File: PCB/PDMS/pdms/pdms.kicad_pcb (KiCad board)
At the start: 2 copper layers, 31 parts, among them IC1 BTS500101TAEATMA1, IC2 BTS500101TAEATMA1, IC3 BTS500101TAEATMA1, IC4 BTS500101TAEATMA1, IC5 BTS500101TAEATMA1, IC6 BTS500101TAEATMA1, IC7 BTS722204ESAXUMA1, IC8 BTS500101TAEATMA1, IC9 BTS500101TAEATMA1

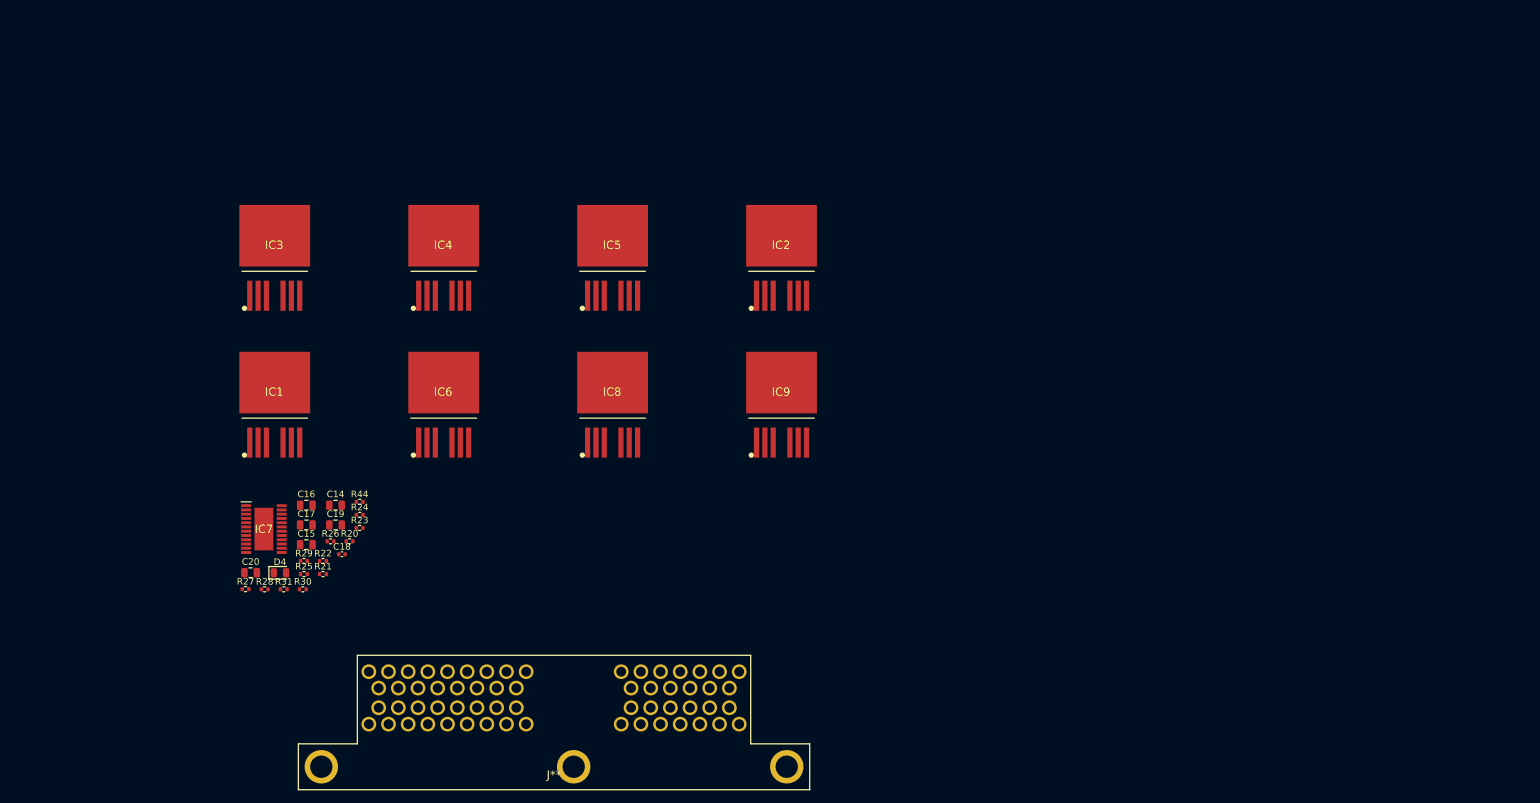
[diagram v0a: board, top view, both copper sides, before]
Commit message: Added MCU section
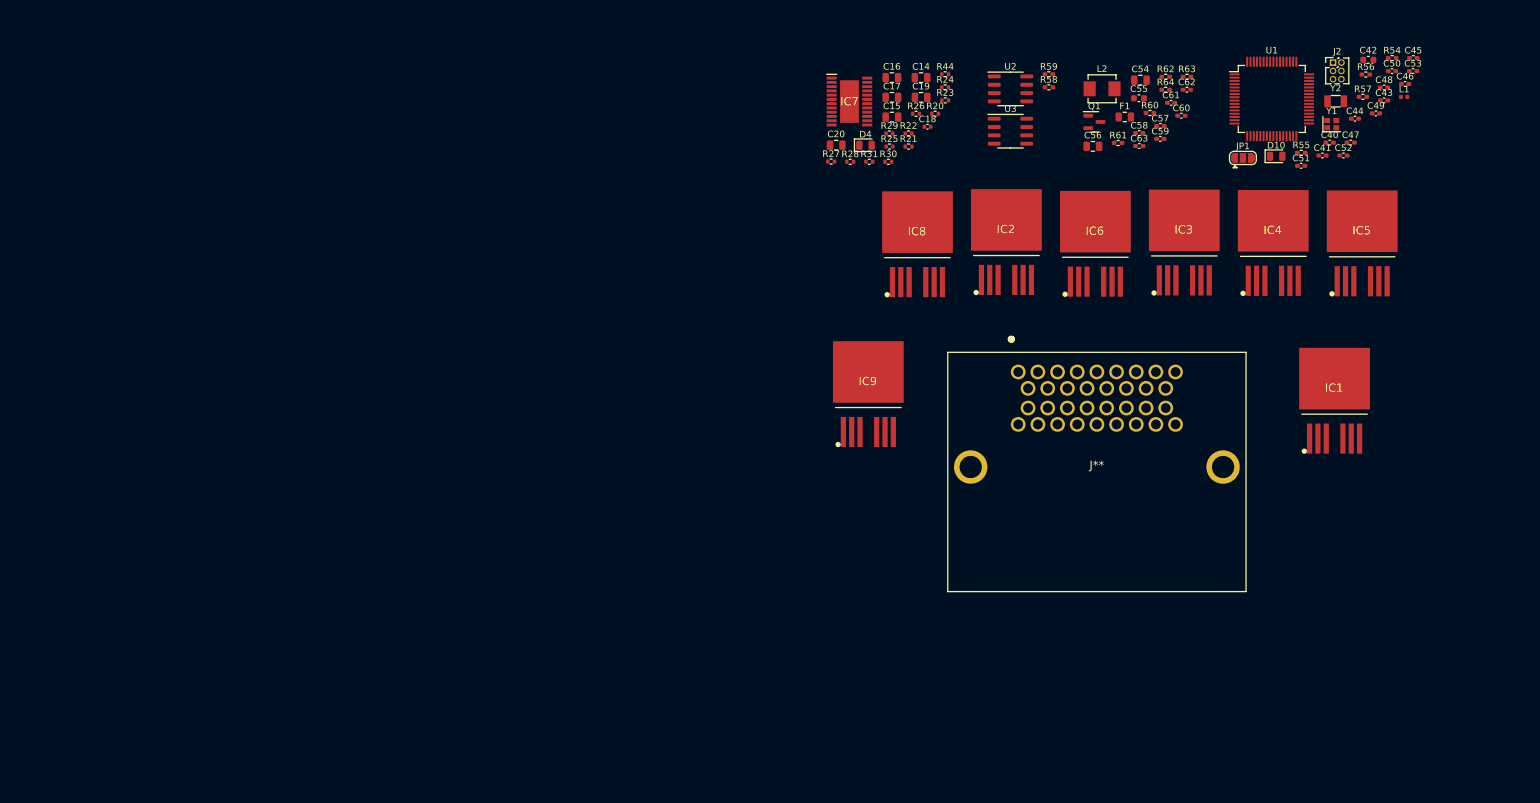
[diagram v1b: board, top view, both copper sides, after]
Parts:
- removed the J** at (76.2, 114.3)
- added C40: 2u2, Capacitor_SMD:C_0402_1005Metric_Pad0.74x0.62mm_HandSolder, F.Cu at (222.8, 33.6)
- added C41: 2u2, Capacitor_SMD:C_0402_1005Metric_Pad0.74x0.62mm_HandSolder, F.Cu at (221.7, 35.6)
- added C42: 4,7uF, Capacitor_SMD:C_0603_1608Metric, F.Cu at (228.7, 21.0)
- added C43: 100nF, Capacitor_SMD:C_0402_1005Metric_Pad0.74x0.62mm_HandSolder, F.Cu at (231.1, 27.2)
- added C44: 100nF, Capacitor_SMD:C_0402_1005Metric_Pad0.74x0.62mm_HandSolder, F.Cu at (226.6, 29.9)
- added C45: 100nF, Capacitor_SMD:C_0402_1005Metric_Pad0.74x0.62mm_HandSolder, F.Cu at (235.5, 20.7)
- added C46: 100nF, Capacitor_SMD:C_0402_1005Metric_Pad0.74x0.62mm_HandSolder, F.Cu at (234.3, 24.6)
- added C47: 100n, Capacitor_SMD:C_0402_1005Metric_Pad0.74x0.62mm_HandSolder, F.Cu at (226.0, 33.6)
- added C48: 10pF, Capacitor_SMD:C_0402_1005Metric_Pad0.74x0.62mm_HandSolder, F.Cu at (231.1, 25.2)
- added C49: 100n, Capacitor_SMD:C_0402_1005Metric_Pad0.74x0.62mm_HandSolder, F.Cu at (229.8, 29.1)
- added C50: 10pF, Capacitor_SMD:C_0402_1005Metric_Pad0.74x0.62mm_HandSolder, F.Cu at (232.3, 22.7)
- added C51: 1u, Capacitor_SMD:C_0402_1005Metric_Pad0.74x0.62mm_HandSolder, F.Cu at (218.4, 37.1)
- added C52: 10pF, Capacitor_SMD:C_0402_1005Metric_Pad0.74x0.62mm_HandSolder, F.Cu at (224.9, 35.6)
- added C53: 10pF, Capacitor_SMD:C_0402_1005Metric_Pad0.74x0.62mm_HandSolder, F.Cu at (235.5, 22.7)
- added C54: 1uF, Capacitor_SMD:C_0805_2012Metric, F.Cu at (193.9, 24.1)
- added C55: 4.7uF, Capacitor_SMD:C_0603_1608Metric, F.Cu at (193.7, 26.8)
- added C56: 22uF, Capacitor_SMD:C_0805_2012Metric, F.Cu at (186.7, 34.2)
- added C57: 1nF, Capacitor_SMD:C_0402_1005Metric_Pad0.74x0.62mm_HandSolder, F.Cu at (196.9, 31.1)
- added C58: 0.1uF, Capacitor_SMD:C_0402_1005Metric_Pad0.74x0.62mm_HandSolder, F.Cu at (193.7, 32.1)
- added C59: 6.8nF, Capacitor_SMD:C_0402_1005Metric_Pad0.74x0.62mm_HandSolder, F.Cu at (196.9, 33.0)
- added C60: 1uF, Capacitor_SMD:C_0402_1005Metric_Pad0.74x0.62mm_HandSolder, F.Cu at (200.2, 29.5)
- added C61: 10pF, Capacitor_SMD:C_0402_1005Metric_Pad0.74x0.62mm_HandSolder, F.Cu at (198.6, 27.5)
- added C62: 22uF, Capacitor_SMD:C_0402_1005Metric_Pad0.74x0.62mm_HandSolder, F.Cu at (201.0, 25.5)
- added C63: 22uF, Capacitor_SMD:C_0402_1005Metric_Pad0.74x0.62mm_HandSolder, F.Cu at (193.7, 34.1)
- added D10: LED_Small, LED_SMD:LED_0805_2012Metric, F.Cu at (214.6, 35.7)
- added F1: Fuse, Fuse:Fuse_0805_2012Metric, F.Cu at (191.5, 29.7)
- added J**: 64372882, PDMS_Additional:64372882, F.Cu at (175.3, 68.6)
- added J2: DBG, Connector_PinHeader_1.27mm:PinHeader_2x03_P1.27mm_Vertical, F.Cu at (223.3, 21.4)
- added JP1: SolderJumper_3_Open, Jumper:SolderJumper-3_P1.3mm_Open_RoundedPad1.0x1.5mm, F.Cu at (209.5, 35.9)
- added L1: 2u7 120m, Inductor_SMD:L_0402_1005Metric, F.Cu at (234.1, 26.6)
- added L2: 2.2uH, Inductor_SMD:L_Vishay_IHLP-1616, F.Cu at (188.1, 25.4)
- added Q1: AO3401A, Package_TO_SOT_SMD:SOT-23, F.Cu at (186.9, 30.4)
- added R54: 2k2, Resistor_SMD:R_0402_1005Metric_Pad0.72x0.64mm_HandSolder, F.Cu at (232.3, 20.7)
- added R55: 2k2, Resistor_SMD:R_0402_1005Metric_Pad0.72x0.64mm_HandSolder, F.Cu at (218.4, 35.1)
- added R56: 1k5, Resistor_SMD:R_0402_1005Metric_Pad0.72x0.64mm_HandSolder, F.Cu at (228.3, 23.2)
- added R57: 1k, Resistor_SMD:R_0402_1005Metric_Pad0.72x0.64mm_HandSolder, F.Cu at (227.8, 26.6)
- added R58: 120, Resistor_SMD:R_0402_1005Metric_Pad0.72x0.64mm_HandSolder, F.Cu at (179.9, 25.2)
- added R59: 120, Resistor_SMD:R_0402_1005Metric_Pad0.72x0.64mm_HandSolder, F.Cu at (179.9, 23.2)
- added R60: 200k, Resistor_SMD:R_0402_1005Metric_Pad0.72x0.64mm_HandSolder, F.Cu at (195.3, 29.1)
- added R61: 20, Resistor_SMD:R_0402_1005Metric_Pad0.72x0.64mm_HandSolder, F.Cu at (190.5, 33.6)
- added R62: 20k, Resistor_SMD:R_0402_1005Metric_Pad0.72x0.64mm_HandSolder, F.Cu at (197.8, 23.6)
- added R63: 13k, Resistor_SMD:R_0402_1005Metric_Pad0.72x0.64mm_HandSolder, F.Cu at (201.0, 23.6)
- added R64: 40.2k, Resistor_SMD:R_0402_1005Metric_Pad0.72x0.64mm_HandSolder, F.Cu at (197.8, 25.5)
- added U1: STM32F405RGTx, Package_QFP:LQFP-64_10x10mm_P0.5mm, F.Cu at (213.9, 26.9)
- added U2: MCP2561-E-SN, Package_SO:SOIC-8_3.9x4.9mm_P1.27mm, F.Cu at (174.1, 25.4)
- added U3: MCP2561-E-SN, Package_SO:SOIC-8_3.9x4.9mm_P1.27mm, F.Cu at (174.1, 31.9)
- added Y1: 16Mhz, Crystal:Crystal_SMD_2016-4Pin_2.0x1.6mm, F.Cu at (223.1, 30.8)
- added Y2: 32KHz, Crystal:Crystal_SMD_3215-2Pin_3.2x1.5mm, F.Cu at (223.7, 27.3)
- IC1, IC2, IC3, IC4, IC5, IC6, IC8, IC9: footprint PDM_Additional:PG-TO263-7-3_3 -> PDMS_Additional:PG-TO263-7-3_3
- moved IC1 161.7 mm to (223.5, 69.6)
- moved IC3 138.8 mm to (200.6, 45.5)
- moved IC4 126.6 mm to (214.2, 45.5)
- moved IC5 114.4 mm to (227.7, 45.6)
- moved C15 110.6 mm to (156.0, 29.7)
- moved C16 110.6 mm to (156.0, 23.7)
- moved C17 110.6 mm to (156.0, 26.7)
- moved C20 110.6 mm to (147.5, 34.0)
- moved D4 110.6 mm to (152.0, 34.0)
- moved R20 110.6 mm to (162.6, 29.2)
- moved R21 110.6 mm to (158.5, 34.2)
- moved R22 110.6 mm to (158.5, 32.2)
- moved R23 110.6 mm to (164.1, 27.1)
- moved R24 110.6 mm to (164.1, 25.2)
- moved R25 110.6 mm to (155.6, 34.2)
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
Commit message: PDMS schematic update
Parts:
- added BZ1: Buzzer, Buzzer_Beeper:Buzzer_Murata_PKLCS1212E, F.Cu at (245.1, 30.5)
- added D11: WS2812B, LED_SMD:LED_WS2812B-2020_PLCC4_2.0x2.0mm, F.Cu at (183.5, 16.9)
- added D12: WS2812B, LED_SMD:LED_WS2812B-2020_PLCC4_2.0x2.0mm, F.Cu at (194.6, 16.9)
- added D13: WS2812B, LED_SMD:LED_WS2812B-2020_PLCC4_2.0x2.0mm, F.Cu at (189.1, 16.9)
- added D14: WS2812B, LED_SMD:LED_WS2812B-2020_PLCC4_2.0x2.0mm, F.Cu at (178.0, 16.9)
- added D15: WS2812B, LED_SMD:LED_WS2812B-2020_PLCC4_2.0x2.0mm, F.Cu at (200.2, 16.9)
- added D16: WS2812B, LED_SMD:LED_WS2812B-2020_PLCC4_2.0x2.0mm, F.Cu at (172.4, 16.9)
- added D17: WS2812B, LED_SMD:LED_WS2812B-2020_PLCC4_2.0x2.0mm, F.Cu at (205.7, 16.9)
- added D18: WS2812B, LED_SMD:LED_WS2812B-2020_PLCC4_2.0x2.0mm, F.Cu at (166.8, 16.9)
- added D19: WS2812B, LED_SMD:LED_WS2812B-2020_PLCC4_2.0x2.0mm, F.Cu at (161.3, 16.9)
- added IC12: TMP126NDCKR, PDM_Additional:SOT65P210X110-6N, F.Cu at (167.6, 38.1)
- added IC13: TMP126NDCKR, PDM_Additional:SOT65P210X110-6N, F.Cu at (162.6, 38.1)
- added IC14: TMP126NDCKR, PDM_Additional:SOT65P210X110-6N, F.Cu at (162.4, 33.9)
- added Q2: MMBT3904, Package_TO_SOT_SMD:SOT-23, F.Cu at (149.9, 19.1)
- added R65: 10k, Resistor_SMD:R_0402_1005Metric, F.Cu at (161.3, 40.9)
- added R66: 10k, Resistor_SMD:R_0402_1005Metric, F.Cu at (164.2, 40.9)
- added R67: 10k, Resistor_SMD:R_0402_1005Metric, F.Cu at (166.1, 33.0)
- added R72: 1k, Resistor_SMD:R_0402_1005Metric, F.Cu at (156.6, 20.0)
- moved IC2 6.49 mm to (167.6, 48.1)
- moved IC3 6.49 mm to (194.7, 48.2)
- moved IC5 6.49 mm to (221.8, 48.3)
- moved IC6 6.49 mm to (181.1, 48.4)
- moved IC4 6.49 mm to (208.3, 48.3)
- moved IC8 6.49 mm to (154.0, 48.5)
- moved C51 6.49 mm to (212.5, 39.9)
- moved R27 3.27 mm to (144.9, 39.2)
- moved R28 3.27 mm to (147.8, 39.2)
- moved R30 3.27 mm to (153.7, 39.2)
- moved R31 3.27 mm to (150.8, 39.2)
- moved IC1 2.54 mm to (221.0, 69.6)
- moved IC9 1.27 mm to (153.7, 68.6)
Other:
- board outline added: 91.4 x 66 mm

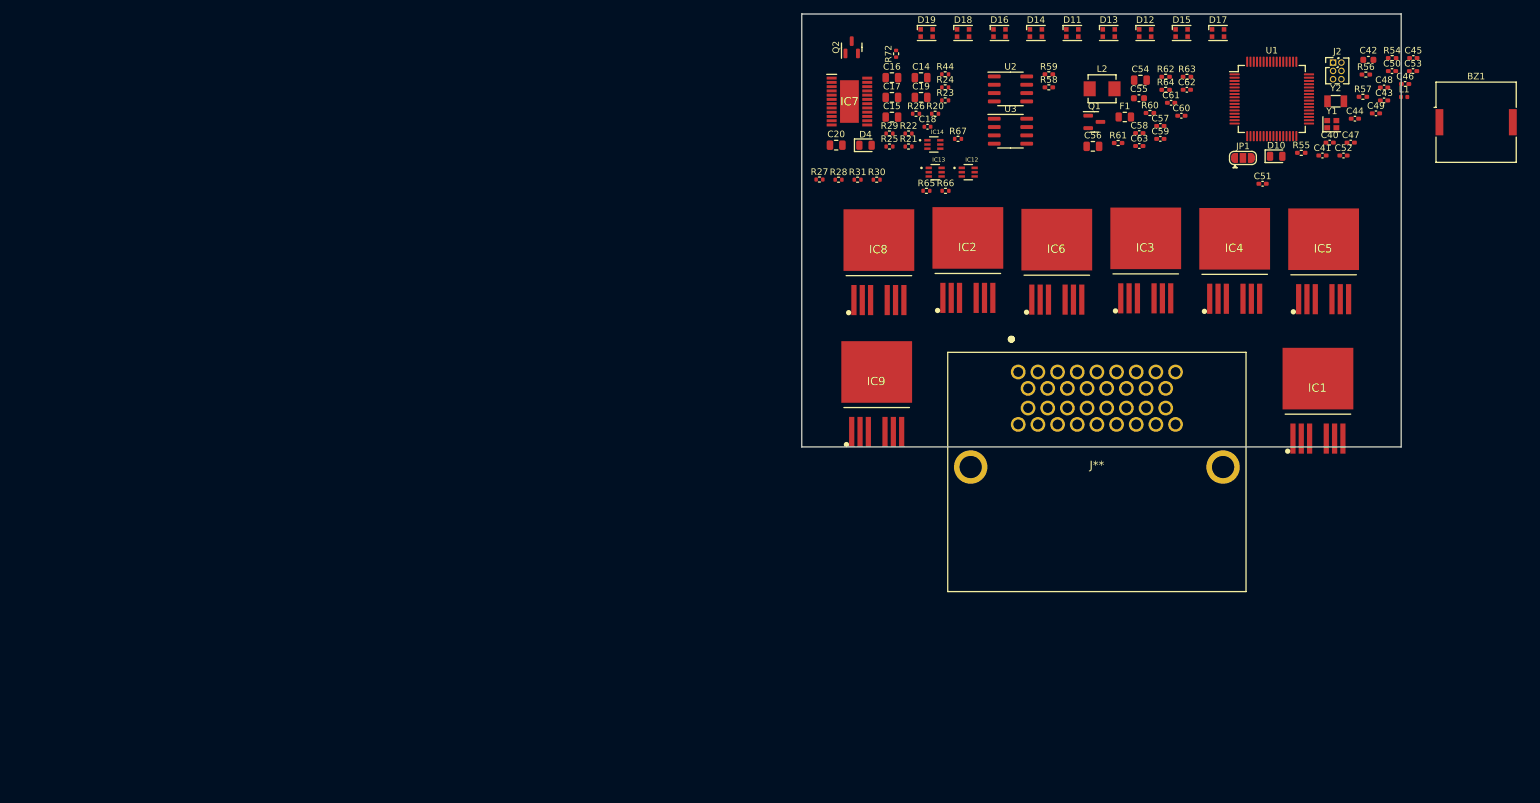
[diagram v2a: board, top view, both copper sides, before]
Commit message: Schematic refactoring
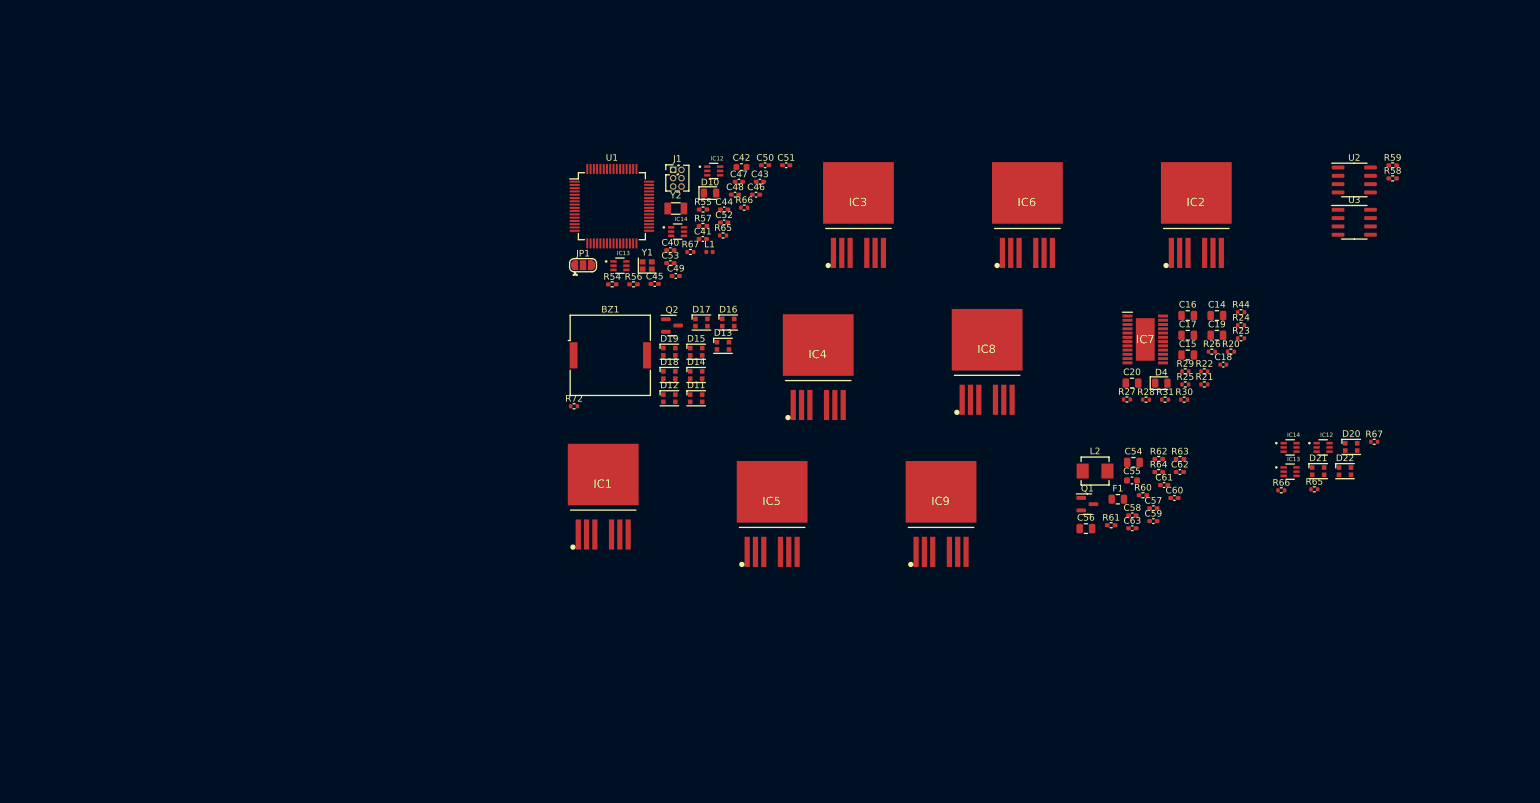
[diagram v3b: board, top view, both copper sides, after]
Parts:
- removed the IC12 at (167.6, 38.1)
- removed the IC13 at (162.6, 38.1)
- removed the IC14 at (162.4, 33.9)
- removed J**: 64372882, PDMS_Additional:64372882
- removed J2: DBG, Connector_PinHeader_1.27mm:PinHeader_2x03_P1.27mm_Vertical
- removed the R65 at (161.3, 40.9)
- removed the R66 at (164.2, 40.9)
- removed the R67 at (166.1, 33.0)
- added D20: WS2812B, LED_SMD:LED_WS2812B-2020_PLCC4_2.0x2.0mm, F.Cu at (226.1, 80.0)
- added D21: WS2812B, LED_SMD:LED_WS2812B-2020_PLCC4_2.0x2.0mm, F.Cu at (221.0, 83.7)
- added D22: WS2812B, LED_SMD:LED_WS2812B-2020_PLCC4_2.0x2.0mm, F.Cu at (225.1, 83.7)
- added IC12: TMP126NDCKR, PDM_Additional:SOT65P210X110-6N, F.Cu at (128.8, 37.9)
- added IC12: TMP126NDCKR, PDM_Additional:SOT65P210X110-6N, F.Cu at (221.8, 80.1)
- added IC13: TMP126NDCKR, PDM_Additional:SOT65P210X110-6N, F.Cu at (114.5, 52.4)
- added IC13: TMP126NDCKR, PDM_Additional:SOT65P210X110-6N, F.Cu at (216.7, 83.8)
- added IC14: TMP126NDCKR, PDM_Additional:SOT65P210X110-6N, F.Cu at (123.3, 47.2)
- added IC14: TMP126NDCKR, PDM_Additional:SOT65P210X110-6N, F.Cu at (216.7, 80.1)
- added J1: DBG, Connector_PinHeader_1.27mm:PinHeader_2x03_P1.27mm_Vertical, F.Cu at (122.6, 37.7)
- added R65: 10k, Resistor_SMD:R_0402_1005Metric, F.Cu at (220.4, 86.5)
- added R65: 10k, Resistor_SMD:R_0402_1005Metric, F.Cu at (130.2, 47.8)
- added R66: 10k, Resistor_SMD:R_0402_1005Metric, F.Cu at (133.5, 43.5)
- added R66: 10k, Resistor_SMD:R_0402_1005Metric, F.Cu at (215.4, 86.6)
- added R67: 10k, Resistor_SMD:R_0402_1005Metric, F.Cu at (229.6, 79.2)
- added R67: 10k, Resistor_SMD:R_0402_1005Metric, F.Cu at (125.3, 50.3)
- moved BZ1 136.8 mm to (113.0, 66.0)
- moved R54 123.9 mm to (113.3, 55.2)
- moved C45 120.7 mm to (119.8, 55.1)
- moved C53 117.0 mm to (122.2, 52.0)
- moved R56 116.2 mm to (116.6, 55.2)
- moved IC1 110.0 mm to (112.0, 84.2)
- moved C49 109.7 mm to (123.0, 53.9)
- moved L1 108.6 mm to (128.2, 50.3)
- moved Y1 106.6 mm to (118.7, 52.3)
- moved R57 102.6 mm to (127.2, 46.3)
- moved JP1 102.0 mm to (108.9, 52.3)
- moved U1 102.0 mm to (113.3, 43.3)
- moved Y2 102.0 mm to (123.0, 43.6)
- moved C40 101.9 mm to (122.2, 50.0)
- moved C46 100.4 mm to (135.3, 41.5)
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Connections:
- net /MCU/CAN_BUS/CAN1_H renamed /CAN_BUS1/CAN1_H
- net /MCU/CAN_BUS/CAN1_L renamed /CAN_BUS1/CAN1_L
- net /MCU/CAN_BUS/CAN2_H renamed /CAN_BUS1/CAN2_H
- net /MCU/CAN_BUS/CAN2_L renamed /CAN_BUS1/CAN2_L
- net /MCU/POWER/PG3V3 renamed /POWER1/PG3V3
- net /POWER_SWITCHES/BTS722204/CSN renamed TB
- net /POWER_SWITCHES/BTS722204/MISO renamed SPI1_MISO
- net /POWER_SWITCHES/BTS722204/MOSI renamed SPI1_MOSI
- net /POWER_SWITCHES/BTS722204/SCLK renamed SPI1_SCK
- net /USER_PERIPHERAL/BUZZ_IN renamed /PERIPHERAL/BUZZ_IN
- net /USER_PERIPHERAL/STATUS_LED_D renamed /PERIPHERAL/STATUS_LED_D
- D19 pad 2: unconnected-(D19-Pad2) -> Net-(D19-Pad2)
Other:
- board outline removed
